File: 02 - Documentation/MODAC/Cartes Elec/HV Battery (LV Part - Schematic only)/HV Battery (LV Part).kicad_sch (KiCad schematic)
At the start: 8 parts, among them K1 AIR+, K2 Precharge relay, K3 AIR-

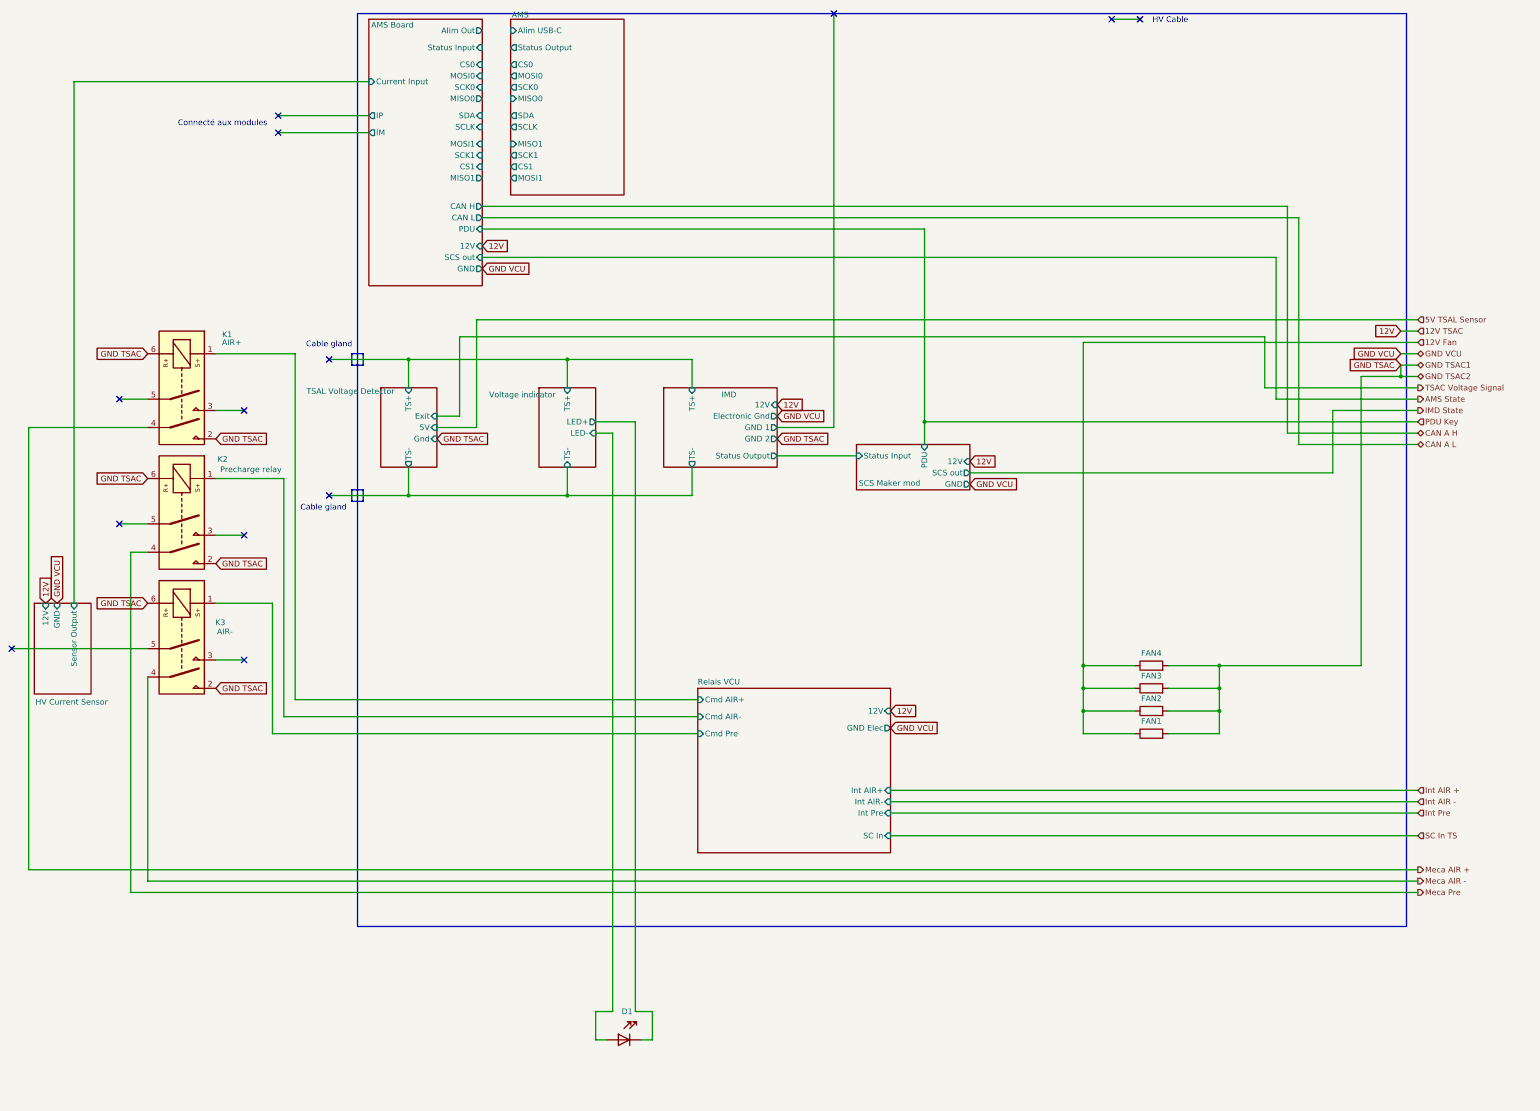
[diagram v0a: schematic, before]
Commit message: Fin TSAC + Correction schema LV batterie
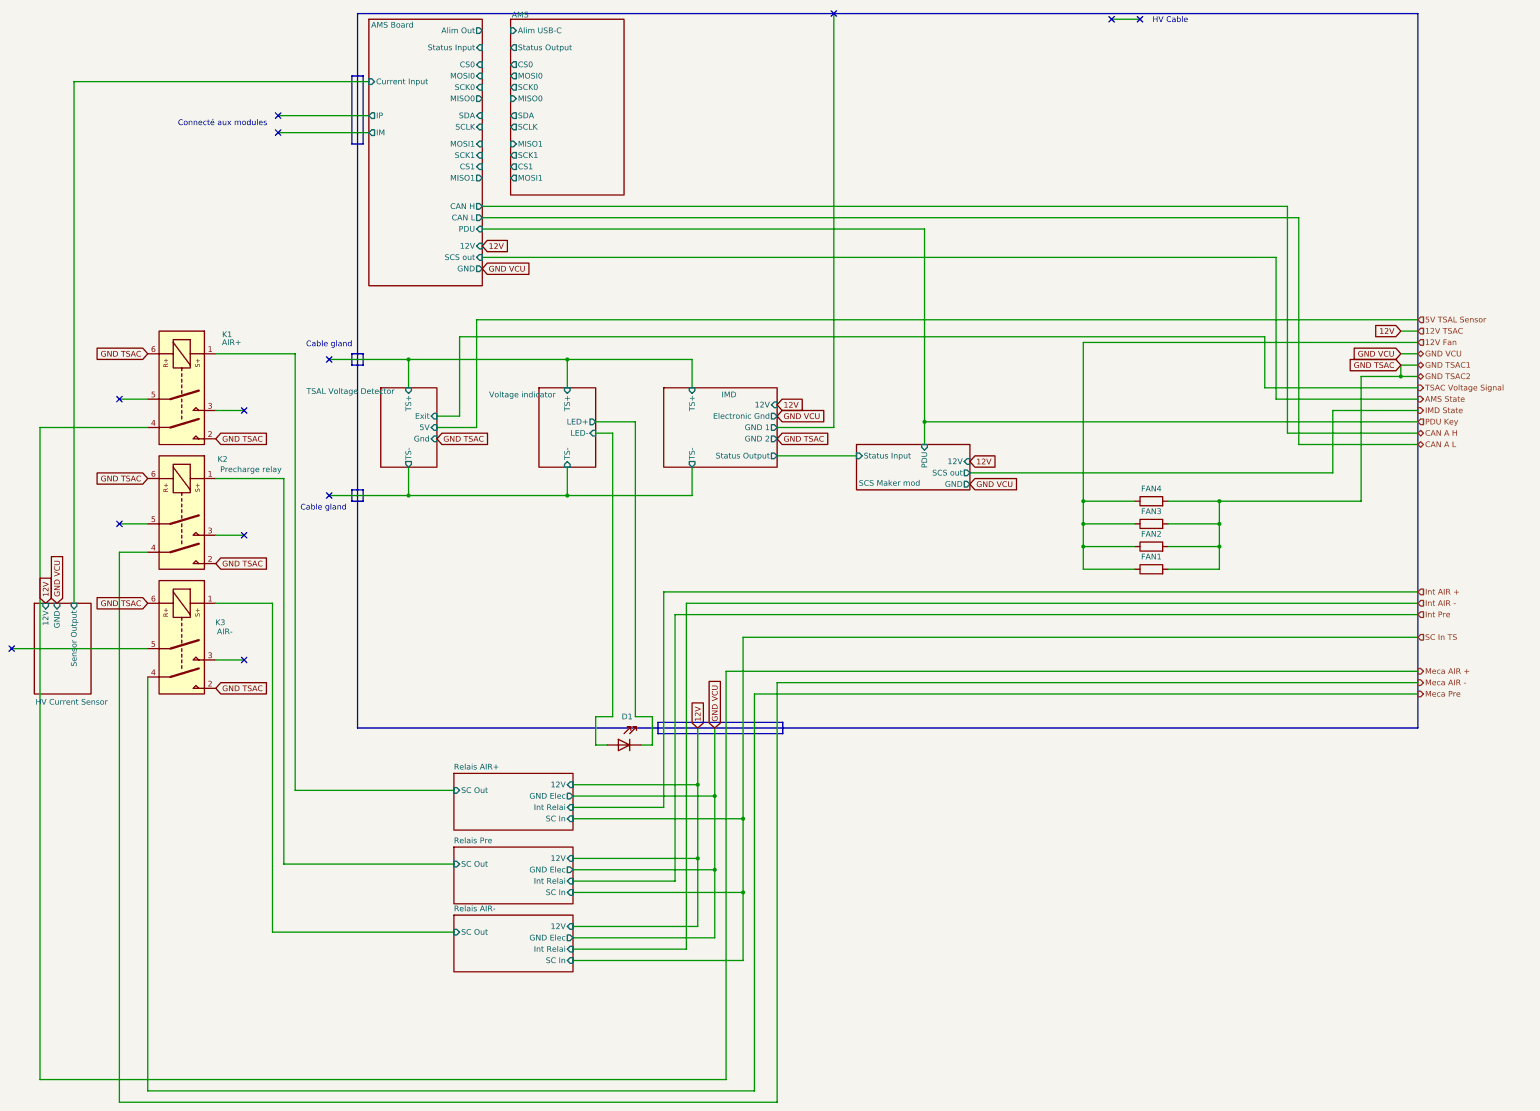
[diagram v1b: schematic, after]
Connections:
- net Meca AIR -: now also K2.4; no longer K3.4
- net Meca Pre: now also K3.4; no longer K2.4
- net Relais VCU/Cmd AIR+ renamed Relais AIR+/SC Out
- net Relais VCU/Cmd AIR- renamed Relais Pre/SC Out
- net Relais VCU/Cmd Pre renamed Relais AIR-/SC Out
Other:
- removed sheet Relais VCU
- added sheet Relais AIR+ (Relais VCU.kicad_sch)
- added sheet Relais AIR- (Relais VCU.kicad_sch)
- added sheet Relais Pre (Relais VCU.kicad_sch)
- moved on the sheet: D1, FAN1, FAN2, FAN3, FAN4
